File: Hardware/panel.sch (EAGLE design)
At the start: 13 parts, among them Q13 BC817-40LT1SMD, Q6 BC807-16LT1SMD

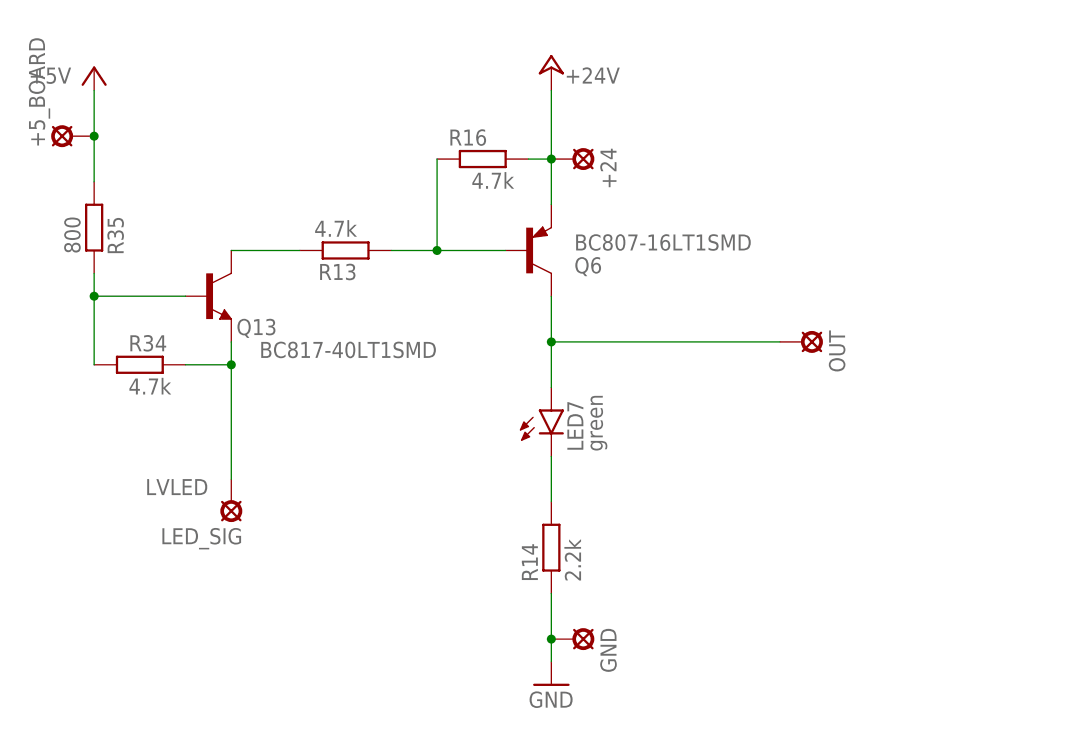
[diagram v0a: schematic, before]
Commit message: проверил работоспособность решения. нес защитный резистор от закоротки выхода на землю, чтоб не сгорал транзистор
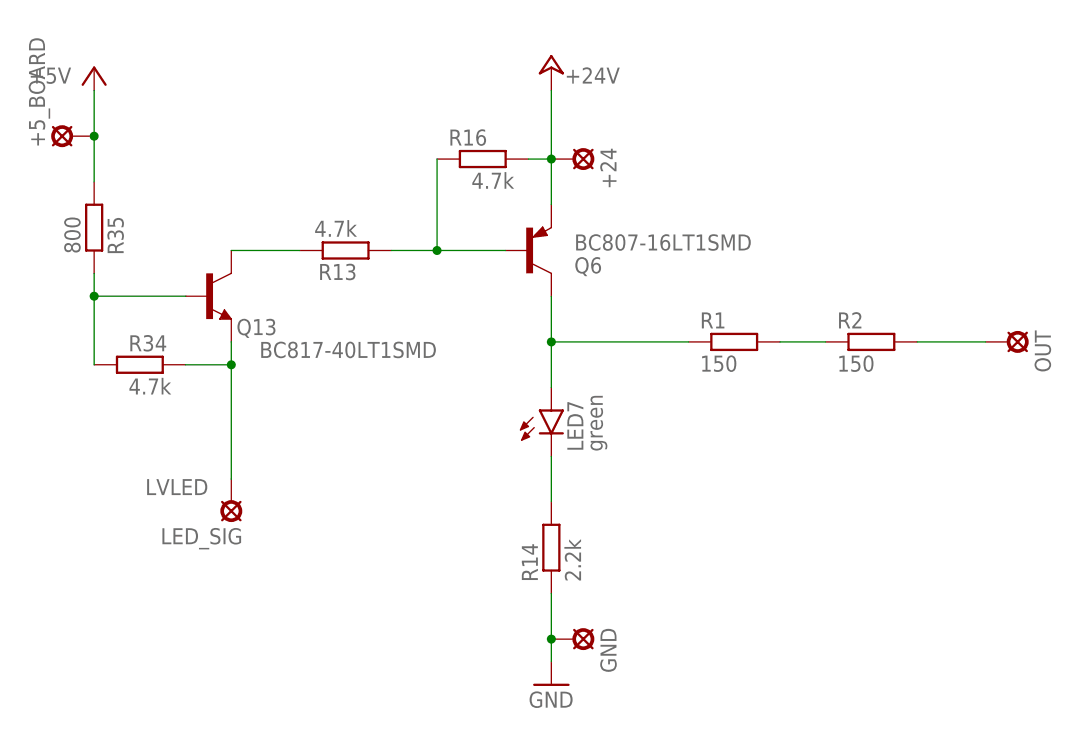
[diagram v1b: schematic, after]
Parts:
- added R1, R2: 150, rcl:R-EU_R2512
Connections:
- new net N$1: R1.2, R2.1
- new net N$2: OUT.MP, R2.2
- net LVLLED_SIG: now also R1.1; no longer OUT.MP
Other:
- moved on the sheet: OUT
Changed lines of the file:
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@@
 <part name="OUT" library="solpad" library_urn="urn:adsk.eagle:library:364" deviceset="LSP10" device="" package3d_urn="urn:adsk.eagle:package:26501/1"/>
 <part name="GND" library="solpad" library_urn="urn:adsk.eagle:library:364" deviceset="LSP10" device="" package3d_urn="urn:adsk.eagle:package:26501/1"/>
+<part name="R1" library="rcl" library_urn="urn:adsk.eagle:library:334" deviceset="R-EU_" device="R2512" package3d_urn="urn:adsk.eagle:package:23545/2" value="150"/>
+<part name="R2" library="rcl" library_urn="urn:adsk.eagle:library:334" deviceset="R-EU_" device="R2512" package3d_urn="urn:adsk.eagle:package:23545/2" value="150"/>
 </parts>
 <sheets>
@@
 <attribute name="NAME" x="46.101" y="54.61" size="1.778" layer="95" rot="R270"/>
 </instance>
-<instance part="OUT" gate="1" x="68.58" y="33.02" smashed="yes" rot="R270">
-<attribute name="NAME" x="71.501" y="34.29" size="1.778" layer="95" rot="R270"/>
+<instance part="OUT" gate="1" x="91.44" y="33.02" smashed="yes" rot="R270">
+<attribute name="NAME" x="94.361" y="34.29" size="1.778" layer="95" rot="R270"/>
 </instance>
 <instance part="GND" gate="1" x="43.18" y="0" smashed="yes" rot="R270">
 <attribute name="NAME" x="46.101" y="1.27" size="1.778" layer="95" rot="R270"/>
+</instance>
+<instance part="R1" gate="G$1" x="60.96" y="33.02" smashed="yes">
+<attribute name="NAME" x="57.15" y="34.5186" size="1.778" layer="95"/>
+<attribute name="VALUE" x="57.15" y="29.718" size="1.778" layer="96"/>
+</instance>
+<instance part="R2" gate="G$1" x="76.2" y="33.02" smashed="yes">
+<attribute name="NAME" x="72.39" y="34.5186" size="1.778" layer="95"/>
+<attribute name="VALUE" x="72.39" y="29.718" size="1.778" layer="96"/>
 </instance>
 </instances>
@@
 <wire x1="40.64" y1="38.1" x2="40.64" y2="33.02" width="0.1524" layer="91"/>
 <wire x1="40.64" y1="33.02" x2="40.64" y2="27.94" width="0.1524" layer="91"/>
-<wire x1="40.64" y1="33.02" x2="66.04" y2="33.02" width="0.1524" layer="91"/>
+<wire x1="40.64" y1="33.02" x2="55.88" y2="33.02" width="0.1524" layer="91"/>
 <junction x="40.64" y="33.02"/>
 <pinref part="LED7" gate="G$1" pin="A"/>
-<pinref part="OUT" gate="1" pin="MP"/>
+<pinref part="R1" gate="G$1" pin="1"/>
 </segment>
 </net>
@@
 </segment>
 </net>
+<net name="N$1" class="0">
+<segment>
+<pinref part="R1" gate="G$1" pin="2"/>
+<pinref part="R2" gate="G$1" pin="1"/>
+<wire x1="71.12" y1="33.02" x2="66.04" y2="33.02" width="0.1524" layer="91"/>
+</segment>
+</net>
+<net name="N$2" class="0">
+<segment>
+<pinref part="OUT" gate="1" pin="MP"/>
+<pinref part="R2" gate="G$1" pin="2"/>
+<wire x1="81.28" y1="33.02" x2="88.9" y2="33.02" width="0.1524" layer="91"/>
+</segment>
+</net>
